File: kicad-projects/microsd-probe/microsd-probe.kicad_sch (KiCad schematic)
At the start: 10 parts, among them J1 Micro_SD_Card_Det2, J2 Micro_SD_Card, J3 Conn_02x06_Odd_Even

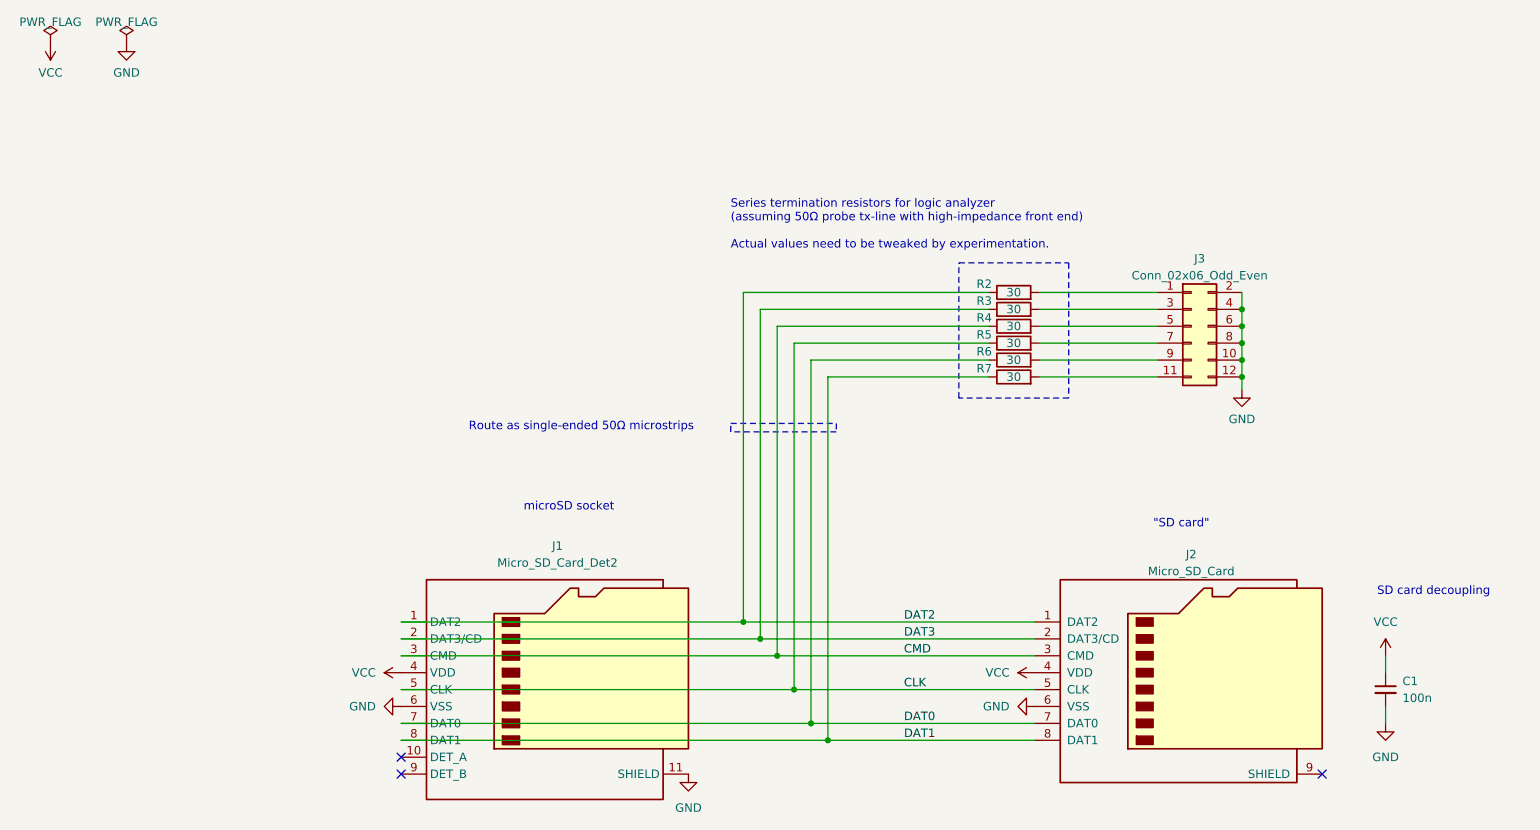
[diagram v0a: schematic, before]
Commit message: microsd-probe: finish 0.1.0 design
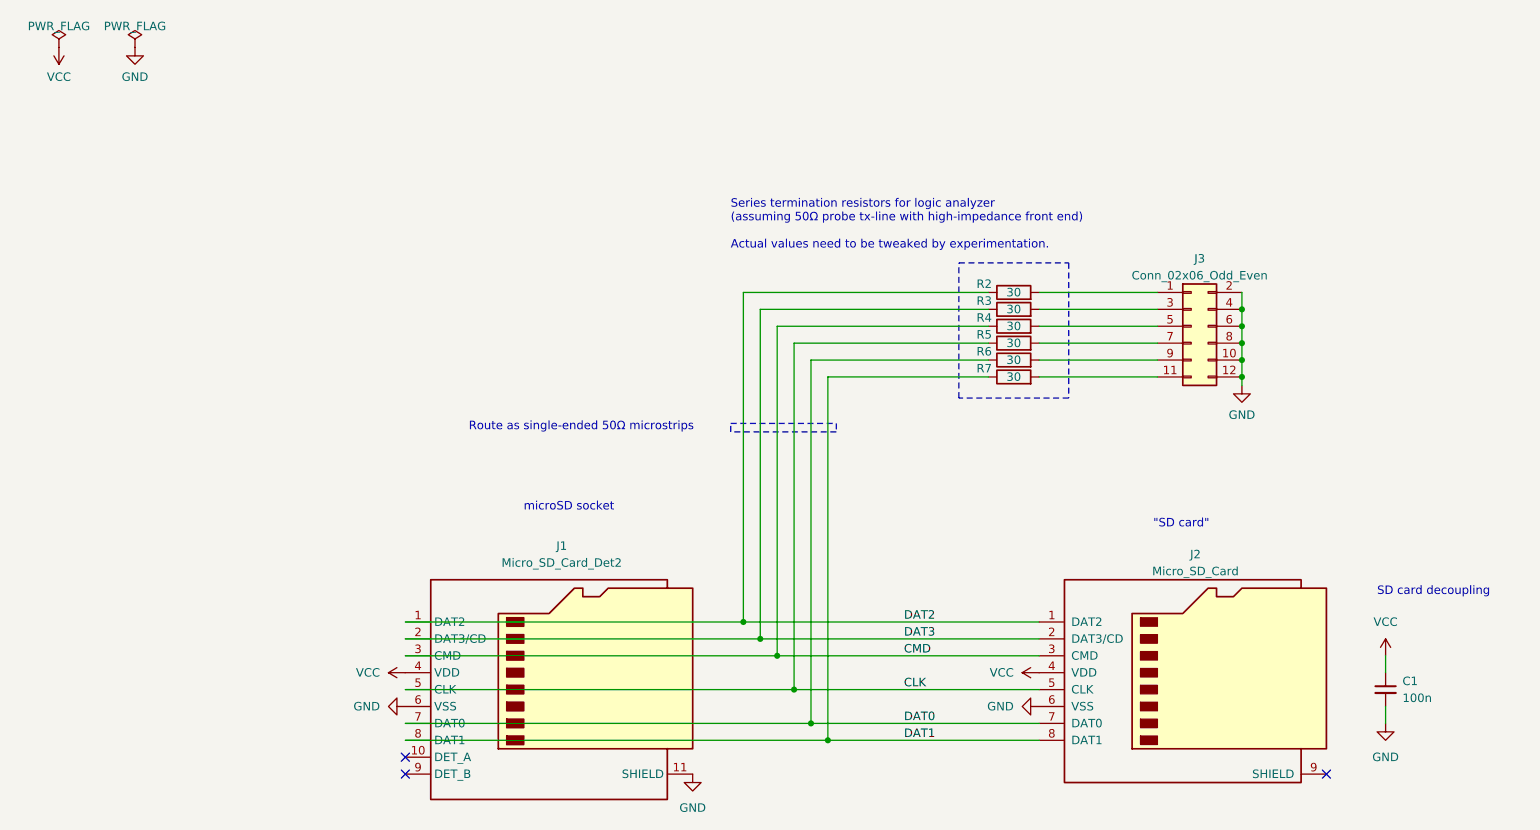
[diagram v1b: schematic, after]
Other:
- title: (none) -> microsd-probe
- moved on the sheet: J1, J2
